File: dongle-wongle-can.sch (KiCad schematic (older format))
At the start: 37 parts, among them J1 MicroLock, J2 PROTO_IO, J3 PROTO_PWR, J4 UART_DEBUG, J5 Conn_ARM_JTAG_SWD_10, J6 PROTO1, J7 PROTO2, SW1 SW_Push, U1 STM32F042F6Px, U2 SN65HVD233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

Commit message: implemented some changes
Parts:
- removed R7: 200, Resistor_SMD:R_0603_1608Metric, symbol Device:R_Small
- added C8: 100n, Capacitor_SMD:C_0603_1608Metric, symbol Device:C_Small
- added C9: 100u, Capacitor_SMD:C_1210_3225Metric, symbol Device:C_Small
- added JP1: RESETJUMP, Jumper:SolderJumper-2_P1.3mm_Bridged_Pad1.0x1.5mm, symbol Device:Jumper_NC_Small
- C6: value 10u -> 100u; footprint Capacitor_SMD:C_0603_1608Metric -> Capacitor_SMD:C_1210_3225Metric; manf# GRM188R6YA106MA73D -> CL32A107MPVNNNE
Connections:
- net GND: now also C8.2, C9.2
- net VDD: now also C9.1
- net nRESET: now also C8.1, JP1.2; no longer SW1.2
- new net: JP1.1, SW1.2
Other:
- moved on the sheet: R6
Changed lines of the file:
@@
 L power:VDD #PWR0103
 U 1 1 5EA2EDFD
-P 8050 5600
-F 0 "#PWR0103" H 8050 5450 50  0001 C CNN
-F 1 "VDD" H 8067 5773 50  0000 C CNN
-F 2 "" H 8050 5600 50  0001 C CNN
-F 3 "" H 8050 5600 50  0001 C CNN
-	1    8050 5600
+P 8300 5600
+F 0 "#PWR0103" H 8300 5450 50  0001 C CNN
+F 1 "VDD" H 8317 5773 50  0000 C CNN
+F 2 "" H 8300 5600 50  0001 C CNN
+F 3 "" H 8300 5600 50  0001 C CNN
+	1    8300 5600
 	1    0    0    -1
 $EndComp
@@
 L Device:R_Small R6
 U 1 1 5EA2F18E
-P 8050 5750
-F 0 "R6" H 8109 5796 50  0000 L CNN
-F 1 "1K" H 8109 5705 50  0000 L CNN
-F 2 "Resistor_SMD:R_0603_1608Metric" H 8050 5750 50  0001 C CNN
-F 3 "" H 8050 5750 50  0001 C CNN
-F 4 "RC0603JR-071KL" H 8050 5750 50  0001 C CNN "manf#"
-	1    8050 5750
-	1    0    0    -1
-$EndComp
-Text GLabel 8250 5900 2    50   Input ~ 0
+P 8300 5750
+F 0 "R6" H 8359 5796 50  0000 L CNN
+F 1 "1K" H 8359 5705 50  0000 L CNN
+F 2 "Resistor_SMD:R_0603_1608Metric" H 8300 5750 50  0001 C CNN
+F 3 "" H 8300 5750 50  0001 C CNN
+F 4 "RC0603JR-071KL" H 8300 5750 50  0001 C CNN "manf#"
+	1    8300 5750
+	1    0    0    -1
+$EndComp
+Text GLabel 8450 5900 2    50   Input ~ 0
 nRESET
 $Comp
@@
 	7400 5900 7400 6000
 Wire Wire Line
-	8050 5600 8050 5650
-Wire Wire Line
-	7900 5900 8050 5900
-Wire Wire Line
-	8050 5850 8050 5900
-Wire Wire Line
-	8250 5900 8050 5900
-Connection ~ 8050 5900
+	8300 5600 8300 5650
+Wire Wire Line
+	8100 5900 8250 5900
+Wire Wire Line
+	8450 5900 8300 5900
+Connection ~ 8250 5900
 $Comp
 L Connector_Generic:Conn_02x04_Odd_Even J1
@@
 L power:VDD #PWR0126
 U 1 1 5ECB86BD
-P 3950 2450
-F 0 "#PWR0126" H 3950 2300 50  0001 C CNN
-F 1 "VDD" H 3968 2623 50  0000 C CNN
-F 2 "" H 3950 2450 50  0001 C CNN
-F 3 "" H 3950 2450 50  0001 C CNN
-	1    3950 2450
-	-1   0    0    1
-$EndComp
-Wire Wire Line
-	3950 2450 3950 2350
+P 3950 1850
+F 0 "#PWR0126" H 3950 1700 50  0001 C CNN
+F 1 "VDD" H 3968 2023 50  0000 C CNN
+F 2 "" H 3950 1850 50  0001 C CNN
+F 3 "" H 3950 1850 50  0001 C CNN
+	1    3950 1850
+	1    0    0    -1
+$EndComp
 Wire Wire Line
 	3950 1850 3850 1850
@@
 Wire Wire Line
 	3850 2350 3950 2350
-Connection ~ 3950 2350
 Wire Wire Line
 	3950 2350 3950 2250
@@
 L power:VDDA #PWR0128
 U 1 1 5EF53BED
-P 8600 4250
-F 0 "#PWR0128" H 8600 4100 50  0001 C CNN
-F 1 "VDDA" H 8617 4423 50  0000 C CNN
-F 2 "" H 8600 4250 50  0001 C CNN
-F 3 "" H 8600 4250 50  0001 C CNN
-	1    8600 4250
-	1    0    0    -1
-$EndComp
-Wire Wire Line
-	8600 4350 8350 4350
-Wire Wire Line
-	8600 4250 8600 4350
+P 8750 4250
+F 0 "#PWR0128" H 8750 4100 50  0001 C CNN
+F 1 "VDDA" H 8767 4423 50  0000 C CNN
+F 2 "" H 8750 4250 50  0001 C CNN
+F 3 "" H 8750 4250 50  0001 C CNN
+	1    8750 4250
+	1    0    0    -1
+$EndComp
 Wire Wire Line
 	8350 4350 8350 4250
@@
 U 1 1 5EFBA513
 P 8350 4550
-F 0 "C7" H 8442 4596 50  0000 L CNN
-F 1 "10u" H 8442 4505 50  0000 L CNN
+F 0 "C7" H 8200 4600 50  0000 L CNN
+F 1 "10u" H 8200 4500 50  0000 L CNN
 F 2 "Capacitor_SMD:C_0603_1608Metric" H 8350 4550 50  0001 C CNN
 F 3 "~" H 8350 4550 50  0001 C CNN
@@
 P 6800 4550
 F 0 "C6" H 6600 4600 50  0000 L CNN
-F 1 "10u" H 6550 4500 50  0000 L CNN
-F 2 "Capacitor_SMD:C_0603_1608Metric" H 6800 4550 50  0001 C CNN
+F 1 "100u" H 6550 4500 50  0000 L CNN
+F 2 "Capacitor_SMD:C_1210_3225Metric" H 6800 4550 50  0001 C CNN
 F 3 "~" H 6800 4550 50  0001 C CNN
-F 4 "GRM188R6YA106MA73D" H 6800 4550 50  0001 C CNN "manf#"
+F 4 "CL32A107MPVNNNE" H 6800 4550 50  0001 C CNN "manf#"
 	1    6800 4550
 	1    0    0    -1
@@
 L power:GND #PWR0129
 U 1 1 5EAEA6ED
-P 8600 4750
-F 0 "#PWR0129" H 8600 4500 50  0001 C CNN
-F 1 "GND" H 8750 4750 50  0000 C CNN
-F 2 "" H 8600 4750 50  0001 C CNN
-F 3 "" H 8600 4750 50  0001 C CNN
-	1    8600 4750
-	1    0    0    -1
-$EndComp
-Wire Wire Line
-	8600 4750 8350 4750
+P 8750 4750
+F 0 "#PWR0129" H 8750 4500 50  0001 C CNN
+F 1 "GND" H 8600 4650 50  0000 C CNN
+F 2 "" H 8750 4750 50  0001 C CNN
+F 3 "" H 8750 4750 50  0001 C CNN
+	1    8750 4750
+	1    0    0    -1
+$EndComp
 Connection ~ 8350 4750
 $Comp
@@
 Wire Wire Line
 	6000 5500 6000 5550
-$Comp
-L Device:R_Small R7
-U 1 1 5EB45853
-P 7250 5550
-F 0 "R7" H 7309 5596 50  0000 L CNN
-F 1 "200" H 7309 5505 50  0000 L CNN
-F 2 "Resistor_SMD:R_0603_1608Metric" H 7250 5550 50  0001 C CNN
-F 3 "" H 7250 5550 50  0001 C CNN
-F 4 "RC0603JR-07200RL" H 7250 5550 50  0001 C CNN "manf#"
-	1    7250 5550
-	1    0    0    -1
-$EndComp
-Text GLabel 7250 5300 0    50   Input ~ 0
-SWDCLK
-$Comp
-L power:GND #PWR0111
-U 1 1 5EB4626B
-P 7250 5750
-F 0 "#PWR0111" H 7250 5500 50  0001 C CNN
-F 1 "GND" H 7255 5577 50  0000 C CNN
-F 2 "" H 7250 5750 50  0001 C CNN
-F 3 "" H 7250 5750 50  0001 C CNN
-	1    7250 5750
-	1    0    0    -1
-$EndComp
-Wire Wire Line
-	7250 5300 7250 5450
-Wire Wire Line
-	7250 5650 7250 5750
+Connection ~ 3950 1850
+$Comp
+L Device:C_Small C8
+U 1 1 5EB1DDC9
+P 7700 6050
+F 0 "C8" V 7750 6100 50  0000 L CNN
+F 1 "100n" V 7850 6100 50  0000 L CNN
+F 2 "Capacitor_SMD:C_0603_1608Metric" H 7700 6050 50  0001 C CNN
+F 3 "~" H 7700 6050 50  0001 C CNN
+F 4 "C0603C104Z3VACTU" H 7700 6050 50  0001 C CNN "manf#"
+	1    7700 6050
+	0    1    1    0
+$EndComp
+Wire Wire Line
+	8250 6050 8250 5900
+Wire Wire Line
+	7600 6050 7500 6050
+Wire Wire Line
+	7500 6050 7500 5900
+Connection ~ 7500 5900
+$Comp
+L Device:Jumper_NC_Small JP1
+U 1 1 5EB395CD
+P 8000 5900
+F 0 "JP1" H 8000 6000 50  0000 C CNN
+F 1 "RESETJUMP" H 8000 5850 50  0000 C CNN
+F 2 "Jumper:SolderJumper-2_P1.3mm_Bridged_Pad1.0x1.5mm" H 8000 5900 50  0001 C CNN
+F 3 "~" H 8000 5900 50  0001 C CNN
+F 4 "true" H 8000 5900 50  0001 C CNN "DNP"
+	1    8000 5900
+	1    0    0    -1
+$EndComp
+Wire Wire Line
+	8300 5850 8300 5900
+Connection ~ 8300 5900
+Wire Wire Line
+	8300 5900 8250 5900
+Wire Wire Line
+	7800 6050 8250 6050
+Wire Wire Line
+	8350 4750 8750 4750
+Wire Wire Line
+	8750 4350 8750 4250
+Wire Wire Line
+	8350 4350 8750 4350
+$Comp
+L Device:C_Small C9
+U 1 1 5EBAB3D6
+P 8750 4550
+F 0 "C9" H 8550 4600 50  0000 L CNN
+F 1 "100u" H 8500 4500 50  0000 L CNN
+F 2 "Capacitor_SMD:C_1210_3225Metric" H 8750 4550 50  0001 C CNN
+F 3 "~" H 8750 4550 50  0001 C CNN
+F 4 "CL32A107MPVNNNE" H 8750 4550 50  0001 C CNN "manf#"
+	1    8750 4550
+	1    0    0    -1
+$EndComp
+Wire Wire Line
+	8750 4750 8750 4650
+Connection ~ 8750 4750
+Wire Wire Line
+	8750 4450 8750 4350
+Connection ~ 8750 4350
 $EndSCHEMATC

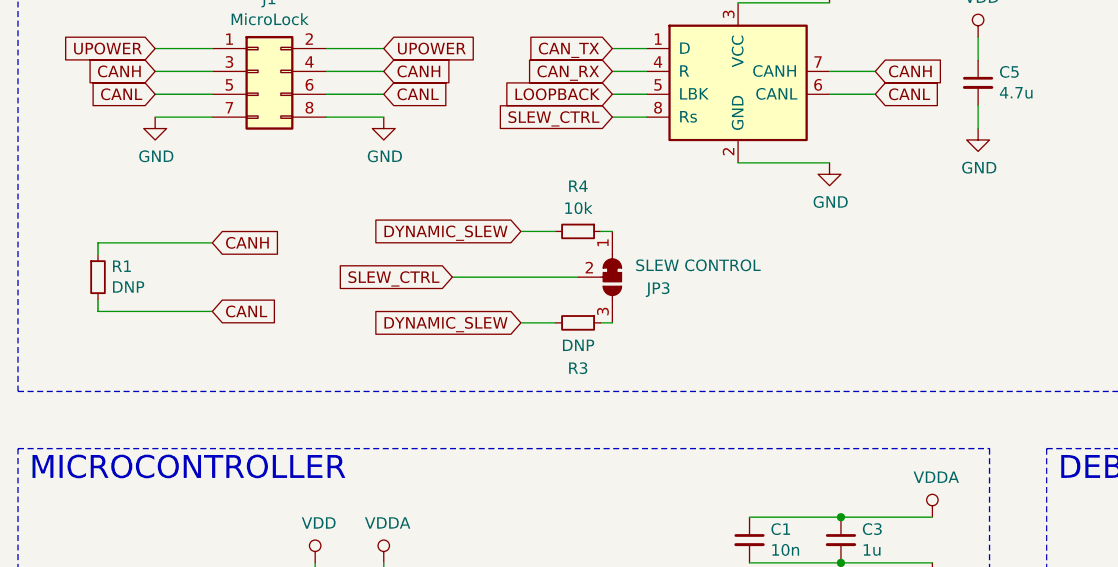
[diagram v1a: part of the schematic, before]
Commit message: added protection diode, and fixed jason's OCD
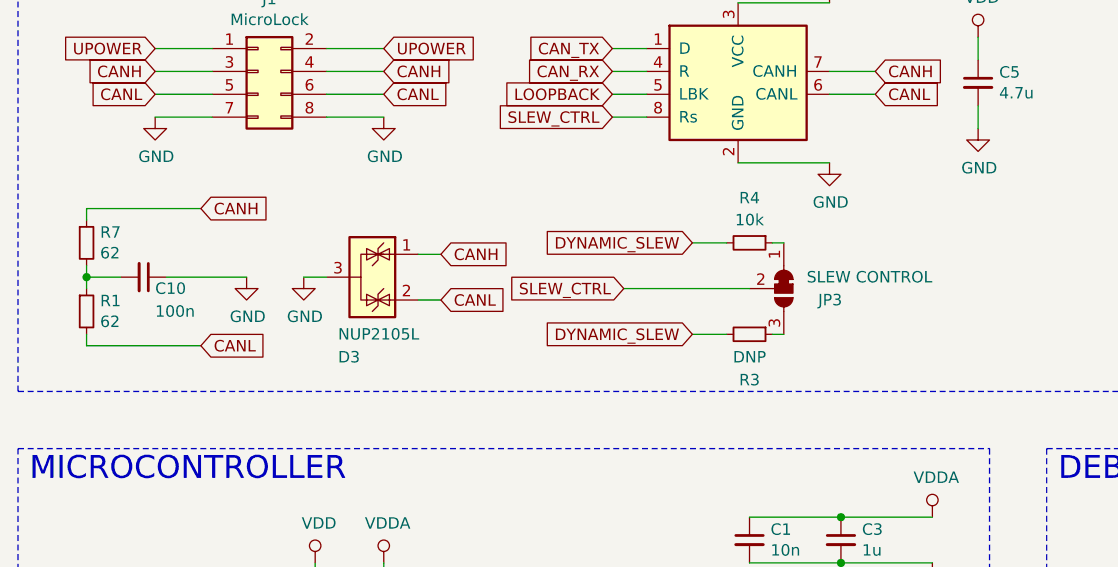
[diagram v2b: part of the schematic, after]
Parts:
- added C10: 100n, Capacitor_SMD:C_0603_1608Metric, symbol Device:C_Small
- added D3: NUP2105L, Package_TO_SOT_SMD:SOT-23, symbol Power_Protection:NUP2105L
- added R7: 62, Resistor_SMD:R_0603_1608Metric, symbol Device:R_Small
- R1: value DNP -> 62; DNP true -> (none); manf# RC0603FR-07120RL -> RC0603FR-0762RL
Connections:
- net CANH: now also D3.1 (K), R7.1; no longer R1.1
- net CANL: now also D3.2 (K)
- net GND: now also C10.1, D3.3 (A)
- new net: C10.2, R1.1, R7.2
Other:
- moved on the sheet: JP3, R1, R3, R4
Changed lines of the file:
@@
 L Device:R_Small R1
 U 1 1 5EA66721
-P 1100 4400
-F 0 "R1" H 1159 4446 50  0000 L CNN
-F 1 "DNP" H 1159 4355 50  0000 L CNN
-F 2 "Resistor_SMD:R_0603_1608Metric" H 1100 4400 50  0001 C CNN
-F 3 "~" H 1100 4400 50  0001 C CNN
-F 4 "RC0603FR-07120RL" H 1100 4400 50  0001 C CNN "manf#"
-F 5 "true" H 1100 4400 50  0001 C CNN "DNP"
-	1    1100 4400
-	1    0    0    -1
-$EndComp
-Text GLabel 1600 4250 2    50   Input ~ 0
+P 1050 4550
+F 0 "R1" H 1109 4596 50  0000 L CNN
+F 1 "62" H 1109 4505 50  0000 L CNN
+F 2 "Resistor_SMD:R_0603_1608Metric" H 1050 4550 50  0001 C CNN
+F 3 "~" H 1050 4550 50  0001 C CNN
+F 4 "RC0603FR-0762RL" H 1050 4550 50  0001 C CNN "manf#"
+F 5 "" H 1050 4550 50  0001 C CNN "DNP"
+	1    1050 4550
+	1    0    0    -1
+$EndComp
+Text GLabel 1550 4100 2    50   Input ~ 0
 CANH
-Text GLabel 1600 4550 2    50   Input ~ 0
+Text GLabel 1550 4700 2    50   Input ~ 0
 CANL
 Wire Wire Line
-	1100 4300 1100 4250
+	1050 4150 1050 4100
 Text GLabel 3350 3700 0    50   Input ~ 0
 SLEW_CTRL
 Wire Wire Line
 	3350 3700 3500 3700
-Text GLabel 2650 4400 0    50   Input ~ 0
+Text GLabel 3400 4450 0    50   Input ~ 0
 SLEW_CTRL
 $Comp
 L Device:R_Small R4
 U 1 1 5EA6B454
-P 3200 4200
-F 0 "R4" V 3004 4200 50  0000 C CNN
-F 1 "10k" V 3100 4200 50  0000 C CNN
-F 2 "Resistor_SMD:R_0603_1608Metric" H 3200 4200 50  0001 C CNN
-F 3 "~" H 3200 4200 50  0001 C CNN
-F 4 "RC0603JR-0710KL" V 3200 4200 50  0001 C CNN "manf#"
-	1    3200 4200
+P 3950 4250
+F 0 "R4" V 3754 4250 50  0000 C CNN
+F 1 "10k" V 3850 4250 50  0000 C CNN
+F 2 "Resistor_SMD:R_0603_1608Metric" H 3950 4250 50  0001 C CNN
+F 3 "~" H 3950 4250 50  0001 C CNN
+F 4 "RC0603JR-0710KL" V 3950 4250 50  0001 C CNN "manf#"
+	1    3950 4250
 	0    1    1    0
 $EndComp
@@
 L Jumper:SolderJumper_3_Bridged12 JP3
 U 1 1 5EA88120
-P 3350 4400
-F 0 "JP3" V 3400 4550 50  0000 L CNN
-F 1 "SLEW CONTROL" V 3300 4500 50  0000 L CNN
-F 2 "Jumper:SolderJumper-3_P1.3mm_Bridged2Bar12_Pad1.0x1.5mm" H 3350 4400 50  0001 C CNN
-F 3 "~" H 3350 4400 50  0001 C CNN
-F 4 "true" H 3350 4400 50  0001 C CNN "DNP"
-	1    3350 4400
+P 4100 4450
+F 0 "JP3" V 4150 4600 50  0000 L CNN
+F 1 "SLEW CONTROL" V 4050 4550 50  0000 L CNN
+F 2 "Jumper:SolderJumper-3_P1.3mm_Bridged2Bar12_Pad1.0x1.5mm" H 4100 4450 50  0001 C CNN
+F 3 "~" H 4100 4450 50  0001 C CNN
+F 4 "true" H 4100 4450 50  0001 C CNN "DNP"
+	1    4100 4450
 	0    1    1    0
 $EndComp
-Text GLabel 2950 4600 0    50   Input ~ 0
+Text GLabel 3700 4650 0    50   Input ~ 0
 DYNAMIC_SLEW
 Text GLabel 2350 3400 2    50   Input ~ 0
@@
 	7450 3700 7600 3700
 Wire Wire Line
-	1100 4550 1600 4550
-Wire Wire Line
-	1100 4550 1100 4500
-Wire Wire Line
-	1600 4250 1100 4250
+	1050 4700 1550 4700
+Wire Wire Line
+	1050 4700 1050 4650
+Wire Wire Line
+	1550 4100 1050 4100
 $Comp
 L Device:C_Small C2
@@
 	1    0    0    -1
 $EndComp
-Text GLabel 2950 4200 0    50   Input ~ 0
+Text GLabel 3700 4250 0    50   Input ~ 0
 DYNAMIC_SLEW
 Wire Wire Line
-	2950 4200 3100 4200
-Wire Wire Line
-	3300 4200 3350 4200
-Wire Wire Line
-	2650 4400 3200 4400
+	3700 4250 3850 4250
+Wire Wire Line
+	4050 4250 4100 4250
+Wire Wire Line
+	3400 4450 3950 4450
 $Comp
 L Device:R_Small R3
 U 1 1 5EA9F0C1
-P 3200 4600
-F 0 "R3" V 3400 4600 50  0000 C CNN
-F 1 "DNP" V 3300 4600 50  0000 C CNN
-F 2 "Resistor_SMD:R_0603_1608Metric" H 3200 4600 50  0001 C CNN
-F 3 "~" H 3200 4600 50  0001 C CNN
-F 4 "RC0603JR-0710KL" V 3200 4600 50  0001 C CNN "manf#"
-F 5 "true" H 3200 4600 50  0001 C CNN "DNP"
-	1    3200 4600
+P 3950 4650
+F 0 "R3" V 4150 4650 50  0000 C CNN
+F 1 "DNP" V 4050 4650 50  0000 C CNN
+F 2 "Resistor_SMD:R_0603_1608Metric" H 3950 4650 50  0001 C CNN
+F 3 "~" H 3950 4650 50  0001 C CNN
+F 4 "RC0603JR-0710KL" V 3950 4650 50  0001 C CNN "manf#"
+F 5 "true" H 3950 4650 50  0001 C CNN "DNP"
+	1    3950 4650
 	0    1    1    0
 $EndComp
 Wire Wire Line
-	3350 4600 3300 4600
-Wire Wire Line
-	3100 4600 2950 4600
+	4100 4650 4050 4650
+Wire Wire Line
+	3850 4650 3700 4650
 $Comp
 L Device:Fuse_Small F1
@@
 	8750 4450 8750 4350
 Connection ~ 8750 4350
+$Comp
+L Device:R_Small R7
+U 1 1 5EB1A007
+P 1050 4250
+F 0 "R7" H 1109 4296 50  0000 L CNN
+F 1 "62" H 1109 4205 50  0000 L CNN
+F 2 "Resistor_SMD:R_0603_1608Metric" H 1050 4250 50  0001 C CNN
+F 3 "~" H 1050 4250 50  0001 C CNN
+F 4 "RC0603FR-0762RL" H 1050 4250 50  0001 C CNN "manf#"
+F 5 "" H 1050 4250 50  0001 C CNN "DNP"
+	1    1050 4250
+	1    0    0    -1
+$EndComp
+Wire Wire Line
+	1050 4450 1050 4400
+$Comp
+L power:GND #PWR01
+U 1 1 5EB3DBBB
+P 1750 4400
+F 0 "#PWR01" H 1750 4150 50  0001 C CNN
+F 1 "GND" H 1755 4227 50  0000 C CNN
+F 2 "" H 1750 4400 50  0001 C CNN
+F 3 "" H 1750 4400 50  0001 C CNN
+	1    1750 4400
+	1    0    0    -1
+$EndComp
+$Comp
+L Device:C_Small C10
+U 1 1 5EB43838
+P 1300 4400
+F 0 "C10" V 1350 4450 50  0000 L CNN
+F 1 "100n" V 1450 4450 50  0000 L CNN
+F 2 "Capacitor_SMD:C_0603_1608Metric" H 1300 4400 50  0001 C CNN
+F 3 "~" H 1300 4400 50  0001 C CNN
+F 4 "C0603C104Z3VACTU" H 1300 4400 50  0001 C CNN "manf#"
+	1    1300 4400
+	0    1    1    0
+$EndComp
+Wire Wire Line
+	1050 4400 1200 4400
+Connection ~ 1050 4400
+Wire Wire Line
+	1050 4400 1050 4350
+Wire Wire Line
+	1400 4400 1750 4400
+$Comp
+L Power_Protection:NUP2105L D3
+U 1 1 5EB5A428
+P 2300 4400
+F 0 "D3" V 2650 4250 50  0000 L CNN
+F 1 "NUP2105L" V 2550 4250 50  0000 L CNN
+F 2 "Package_TO_SOT_SMD:SOT-23" H 2525 4350 50  0001 L CNN
+F 3 "http://www.onsemi.com/pub_link/Collateral/NUP2105L-D.PDF" H 2425 4525 50  0001 C CNN
+F 4 "NUP2105LT1G" H 2300 4400 50  0001 C CNN "manf#"
+	1    2300 4400
+	0    1    1    0
+$EndComp
+Text GLabel 2600 4300 2    50   Input ~ 0
+CANH
+$Comp
+L power:GND #PWR02
+U 1 1 5EB9EA42
+P 2000 4400
+F 0 "#PWR02" H 2000 4150 50  0001 C CNN
+F 1 "GND" H 2005 4227 50  0000 C CNN
+F 2 "" H 2000 4400 50  0001 C CNN
+F 3 "" H 2000 4400 50  0001 C CNN
+	1    2000 4400
+	1    0    0    -1
+$EndComp
+Wire Wire Line
+	2000 4400 2100 4400
+Text GLabel 2600 4500 2    50   Input ~ 0
+CANL
+Wire Wire Line
+	2600 4500 2500 4500
+Wire Wire Line
+	2500 4300 2600 4300
 $EndSCHEMATC

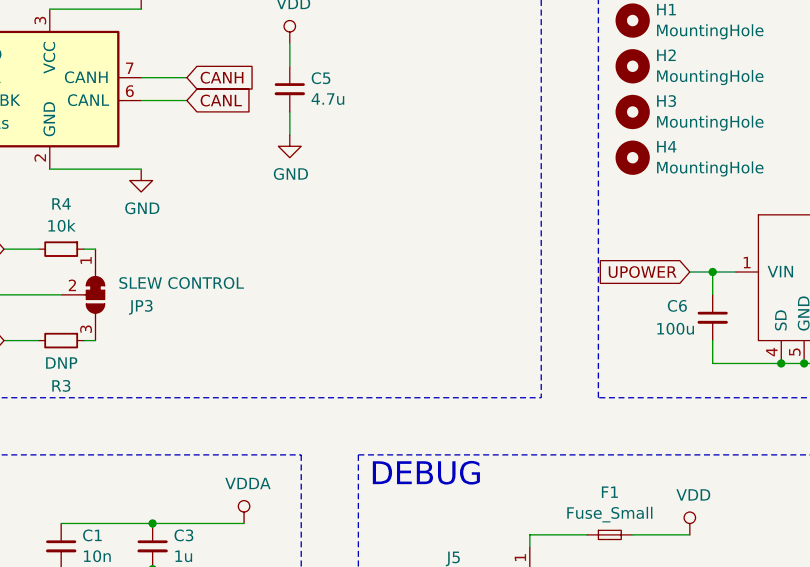
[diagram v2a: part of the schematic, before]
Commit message: add tp (expensive) on tx and rx
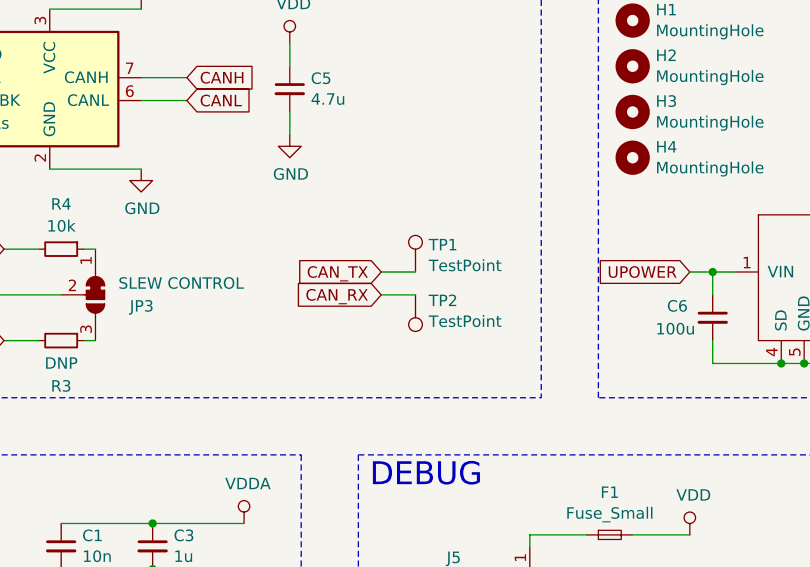
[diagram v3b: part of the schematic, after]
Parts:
- added TP1, TP2: TestPoint, TestPoint:TestPoint_Pad_1.0x1.0mm, symbol Connector:TestPoint
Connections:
- net CAN_RX: now also TP2.1
- net CAN_TX: now also TP1.1
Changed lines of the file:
@@
 Wire Wire Line
 	2500 4300 2600 4300
+Text GLabel 5350 4450 0    50   Input ~ 0
+CAN_RX
+Text GLabel 5350 4350 0    50   Input ~ 0
+CAN_TX
+$Comp
+L Connector:TestPoint TP1
+U 1 1 5EBFFEC6
+P 5500 4350
+F 0 "TP1" H 5558 4468 50  0000 L CNN
+F 1 "TestPoint" H 5558 4377 50  0000 L CNN
+F 2 "TestPoint:TestPoint_Pad_1.0x1.0mm" H 5700 4350 50  0001 C CNN
+F 3 "~" H 5700 4350 50  0001 C CNN
+F 4 "true" H 5500 4350 50  0001 C CNN "DNP"
+	1    5500 4350
+	1    0    0    -1
+$EndComp
+$Comp
+L Connector:TestPoint TP2
+U 1 1 5EC002C9
+P 5500 4450
+F 0 "TP2" H 5442 4476 50  0000 R CNN
+F 1 "TestPoint" H 5442 4567 50  0000 R CNN
+F 2 "TestPoint:TestPoint_Pad_1.0x1.0mm" H 5700 4450 50  0001 C CNN
+F 3 "~" H 5700 4450 50  0001 C CNN
+F 4 "true" H 5500 4450 50  0001 C CNN "DNP"
+	1    5500 4450
+	-1   0    0    1
+$EndComp
+Wire Wire Line
+	5350 4350 5500 4350
+Wire Wire Line
+	5500 4450 5350 4450
 $EndSCHEMATC
